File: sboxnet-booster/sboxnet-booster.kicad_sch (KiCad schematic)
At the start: 72 parts, among them J1 sboxnet-stecker_02x17, J2 cliff_FCR681465P_audiobuchse, J3 Conn_01x02_Male, J4 Conn_01x02_Male, J5 Screw_Terminal_01x04, J6 Screw_Terminal_01x04, SW1 Öffner, U2 L78L12_SOT89, U3 SN65HVD230, U4 l6206

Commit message: entwurf fuer sboxnet-booster
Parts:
- removed C6: 220n, Capacitor_SMD:C_1206_3216Metric, symbol Device:C
- removed C8: 22u/50v, Capacitor_THT:CP_Radial_D5.0mm_P2.00mm, symbol Device:CP
- removed SW1: Öffner, Connector_PinHeader_2.54mm:PinHeader_1x03_P2.54mm_Vertical, symbol Switch:SW_SPDT
- added J7: Conn_01x02_Male, Connector_PinHeader_2.54mm:PinHeader_1x02_P2.54mm_Vertical, symbol Connector:Conn_01x02_Male
- R1, R11, R12, R16, R17, R18, R19, R2, R20, R22, R23, R24, R3, R4, R5, R6, R7, R8, R9: footprint Resistor_SMD:R_1206_3216Metric -> Resistor_SMD:R_1206_3216Metric_Pad1.30x1.75mm_HandSolder
- R26, R28: footprint Resistor_THT:R_Axial_Power_L38.0mm_W9.0mm_P45.72mm -> Resistor_SMD:R_1206_3216Metric_Pad1.30x1.75mm_HandSolder
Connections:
- net DCC_IN: no longer J1.21 (Pin_21)
- net GND: now also J7.1 (Pin_1)
- net at R6.1, R7.2: now also J7.2 (Pin_2)
- net at U3.4 (R): now also J1.21 (Pin_21)
- net at TP7.1: now also D14.1 (K), D15.2 (A), R24.2
- no-connect marks 16 -> 15
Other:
- moved on the sheet: J1, R22, R9, U3

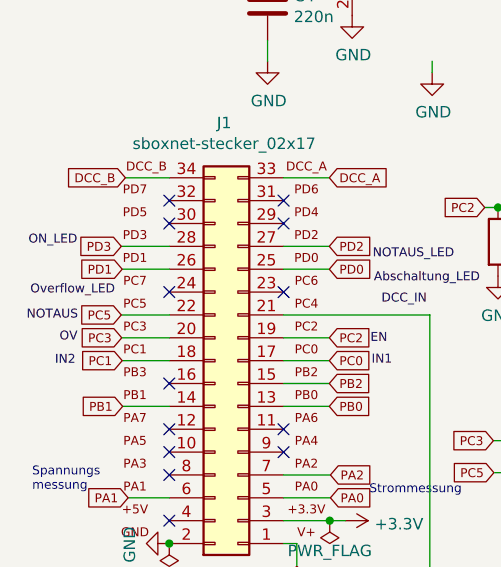
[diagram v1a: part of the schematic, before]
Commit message: booster testpoint pc7, circuit board for out* pins to 1mm
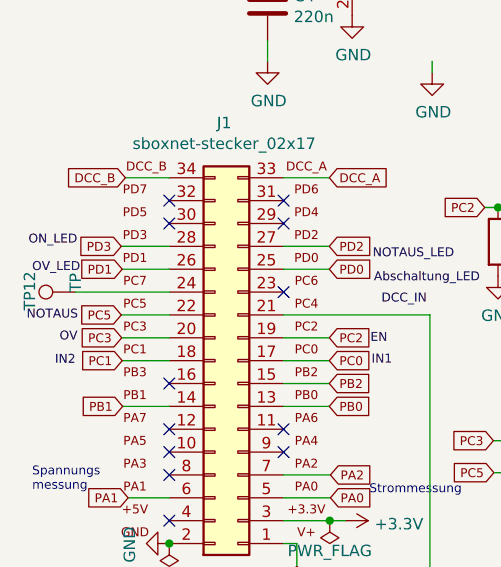
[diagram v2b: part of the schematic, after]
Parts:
- added TP12: TP, Connector_PinHeader_2.54mm:PinHeader_1x01_P2.54mm_Vertical, symbol Connector:TestPoint
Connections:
- net at J1.24 (Pin_24): now also TP12.1
- no-connect marks 15 -> 14
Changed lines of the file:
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@@
   )
   (no_connect (at 27.94 122.174))
-  (no_connect (at 27.94 96.774))
   (no_connect (at 27.94 89.154))
   (no_connect (at 27.94 117.094))
@@
     (stroke (width 0) (type default) (color 0 0 0 0))
   )
+  (wire (pts (xy 17.526 96.774) (xy 27.94 96.774))
+    (stroke (width 0) (type default) (color 0 0 0 0))
+  )
   (wire (pts (xy 40.64 119.634) (xy 45.847 119.634))
     (stroke (width 0) (type default) (color 0 0 0 0))
@@
     (effects (font (size 0.9906 0.9906)) (justify left bottom))
   )
-  (label "Overflow_LED" (at 12.4968 97.2312 0)
+  (label "OV_LED" (at 12.7 94.742 0)
     (effects (font (size 0.9906 0.9906)) (justify left bottom))
   )
@@
     (pin "3")
   )
+  (symbol (lib_id "Connector:TestPoint") (at 17.526 96.774 90) (unit 1)
+    (in_bom yes) (on_board yes)
+    (property "Reference" "TP12" (id 0) (at 12.446 98.806 0)
+      (effects (font (size 1.27 1.27)) (justify left))
+    )
+    (property "Value" "TP" (id 1) (at 17.526 96.774 0)
+      (effects (font (size 1.27 1.27)) (justify left))
+    )
+    (property "Footprint" "Connector_PinHeader_2.54mm:PinHeader_1x01_P2.54mm_Vertical" (id 2) (at 17.526 91.694 0)
+      (effects (font (size 1.27 1.27)) hide)
+    )
+    (property "Datasheet" "~" (id 3) (at 17.526 91.694 0)
+      (effects (font (size 1.27 1.27)) hide)
+    )
+    (pin "1")
+  )
   (symbol (lib_id "Connector:Conn_01x02_Male") (at 84.328 128.016 180) (unit 1)
     (in_bom yes) (on_board yes)
@@
       (reference "TP11") (unit 1) (value "TestPoint") (footprint "Connector_PinHeader_2.54mm:PinHeader_1x01_P2.54mm_Vertical")
     )
+    (path "/b94d61c6-7bef-4764-8cd1-ee71fe366fe4"
+      (reference "TP12") (unit 1) (value "TP") (footprint "Connector_PinHeader_2.54mm:PinHeader_1x01_P2.54mm_Vertical")
+    )
     (path "/00000000-0000-0000-0000-00005f0cf06c"

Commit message: kleiner booster
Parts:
- removed C4: 220n, Capacitor_SMD:C_1206_3216Metric, symbol Device:C
- removed U2: L78L12_SOT89, Package_TO_SOT_SMD:SOT-89-3, symbol Regulator_Linear:L78L12_SOT89
- D14, D15: footprint Diode_SMD:D_SOD-323 -> Diode_SMD:D_SOD-123F
- R25, R27: footprint Resistor_THT:R_Axial_Power_L38.0mm_W9.0mm_P45.72mm -> Resistor_THT:R_Axial_DIN0614_L14.3mm_D5.7mm_P15.24mm_Horizontal
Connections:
- net +12V: no longer names the net of J1.1 (Pin_1)
- no-connect marks 14 -> 15
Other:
- moved on the sheet: C7

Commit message: shrink booster
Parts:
- C5: value 47n -> 100n
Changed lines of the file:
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@@
     (in_bom yes) (on_board yes)
     (property "Reference" "C5" (id 0) (at 80.1878 47.498 90))
-    (property "Value" "47n" (id 1) (at 77.851 47.244 90))
+    (property "Value" "100n" (id 1) (at 77.851 47.244 90))
     (property "Footprint" "Capacitor_SMD:C_1206_3216Metric" (id 2) (at 72.8218 43.688 0)
       (effects (font (size 1.27 1.27)) hide)
@@
     )
     (path "/00000000-0000-0000-0000-00005f02019e"
-      (reference "C5") (unit 1) (value "47n") (footprint "Capacitor_SMD:C_1206_3216Metric")
+      (reference "C5") (unit 1) (value "100n") (footprint "Capacitor_SMD:C_1206_3216Metric")
     )
     (path "/00000000-0000-0000-0000-00005dbbe48c"
